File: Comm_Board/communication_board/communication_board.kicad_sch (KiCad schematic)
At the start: 40 parts, among them J1 USB_IN, J2 IMU, J3 Mini Fuse Socket, J4 XM_conn, U1 FE1.1s, U2 FT232RL, U3 FT232RL, U4 MAX485E, Y1 Crystal 12MHz - ECS

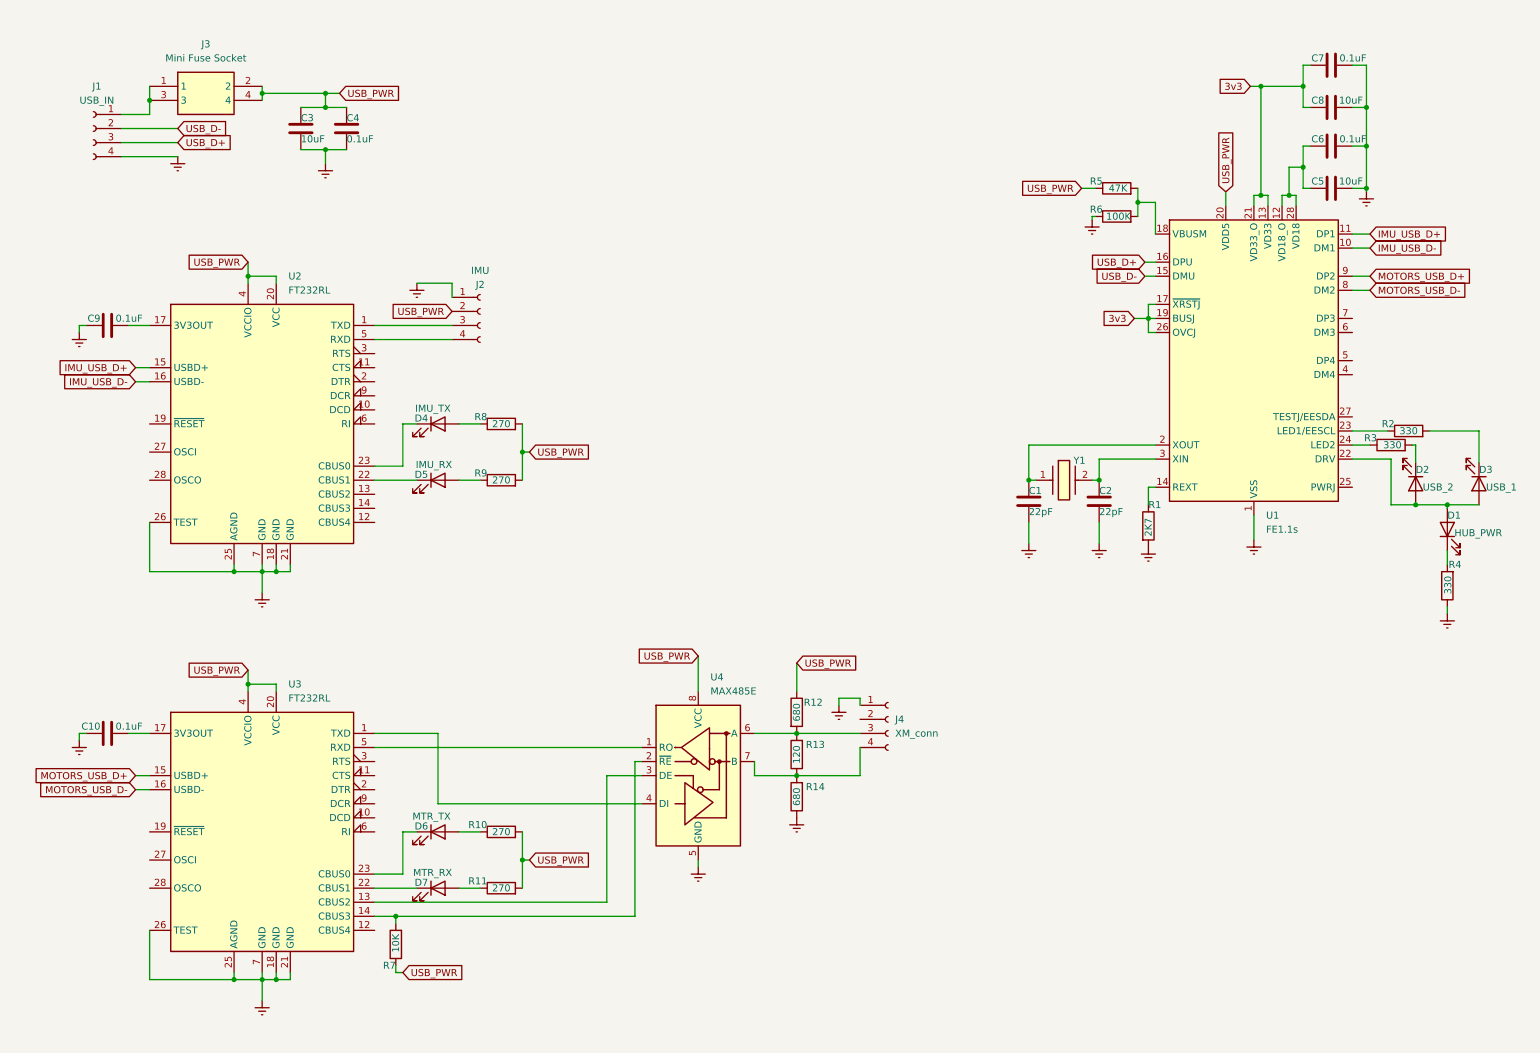
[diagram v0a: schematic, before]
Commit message: Organizing Comm board folder
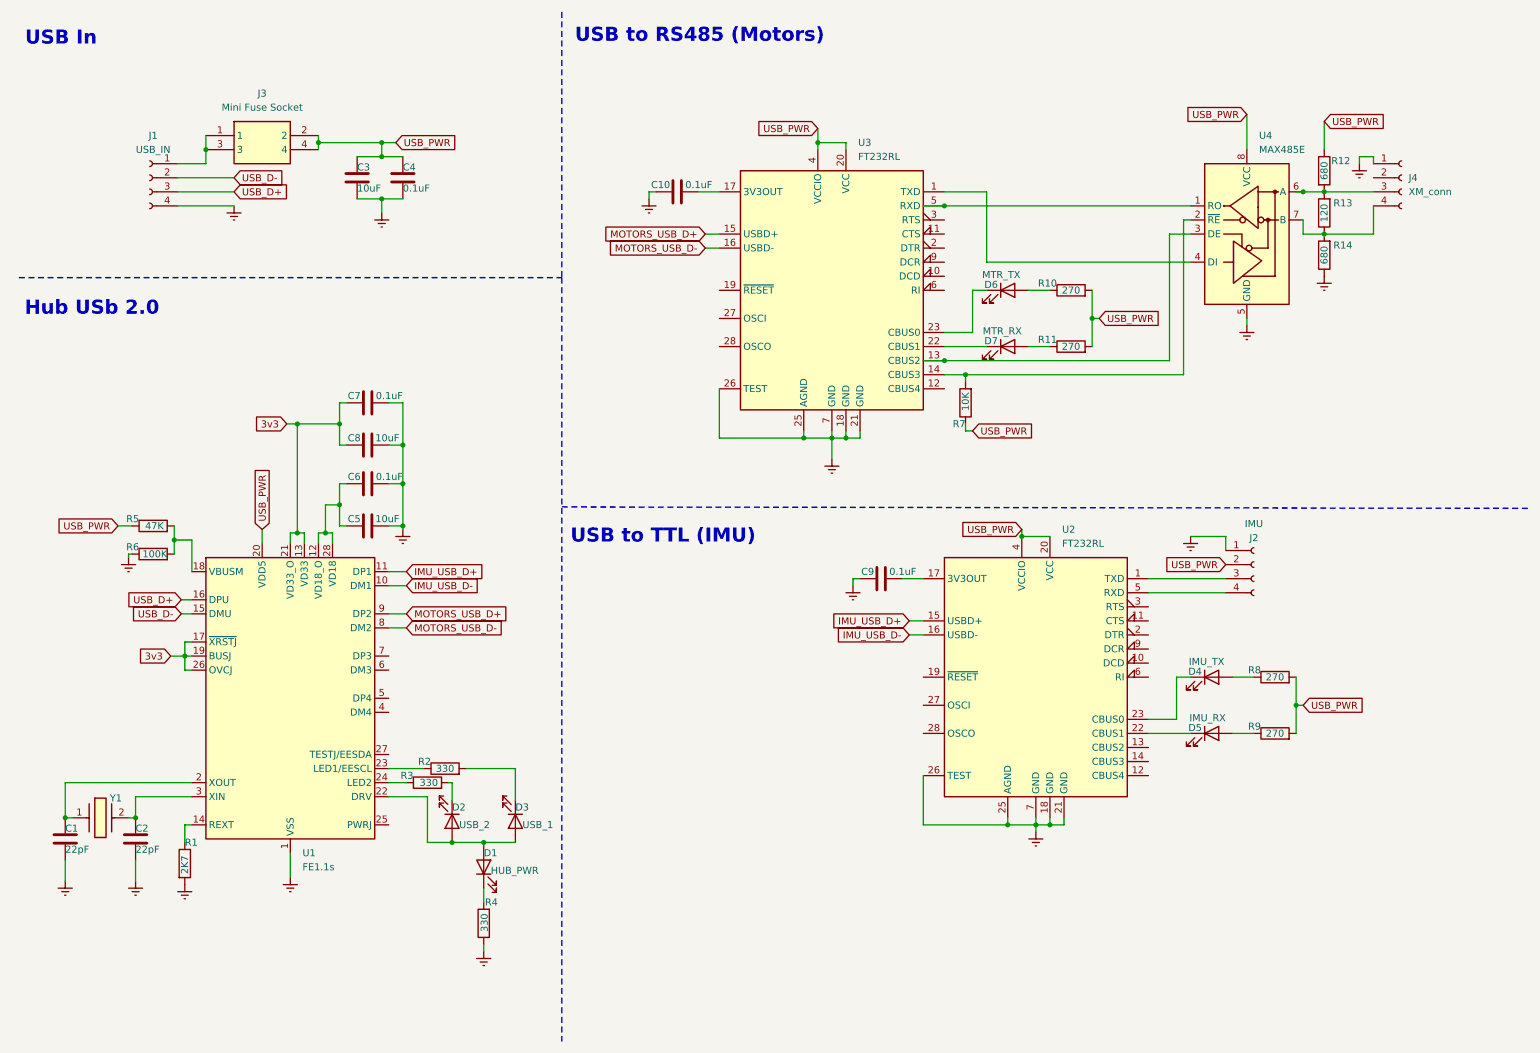
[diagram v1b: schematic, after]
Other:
- note added: "Hub USb 2.0"
- note added: "USB In"
- note added: "USB to RS485 (Motors)"
- note added: "USB to TTL (IMU)"
- moved on the sheet: C1, C10, C2, C3, C4, C5, C6, C7, C8, C9, D1, D2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
